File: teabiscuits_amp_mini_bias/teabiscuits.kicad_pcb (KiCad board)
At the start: 2 copper layers, 25 x 20 mm, 15 parts, among them J1 Conn_Coaxial, J2 Conn_Coaxial, J3 Conn_01x03_Male, J4 Conn_Coaxial, U2 LMP7721, U3 OP07

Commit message: Misc updates
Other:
- board text added: "TeaBisMB r2"
- board text removed: "TeaBisMB r1"
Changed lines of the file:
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@@
   (gr_line (start 152 140.75) (end 152 132.31) (layer Edge.Cuts) (width 0.05))
   (gr_line (start 177 128.75) (end 177 128.81) (layer Edge.Cuts) (width 0.05))
-  (gr_text "TeaBisMB r1" (at 156.5 143.25) (layer F.SilkS)
+  (gr_text "TeaBisMB r2" (at 156.5 143.25) (layer F.SilkS)
     (effects (font (size 0.5 0.5) (thickness 0.125)))
   )
@@
   (segment (start 165 142.6875) (end 165 142.475) (width 0.25) (layer B.Cu) (net 7))
   (segment (start 165 142.475) (end 165.5 141.975) (width 0.25) (layer B.Cu) (net 7))
-  (segment (start 170.55 130.56) (end 170.55 130.55) (width 0.25) (layer F.Cu) (net 12))
-  (segment (start 170.55 130.55) (end 170.5 130.5) (width 0.25) (layer F.Cu) (net 12))
   (segment (start 171 132.12) (end 171.481587 132.12) (width 0.25) (layer F.Cu) (net 11))
   (segment (start 171.481587 132.12) (end 171.886587 132.525) (width 0.25) (layer F.Cu) (net 11))
   (segment (start 158 132.12) (end 158 132.1) (width 0.25) (layer F.Cu) (net 11))
-  (via (at 175.75 144.5) (size 1.11) (drill 1.1) (layers F.Cu B.Cu) (net 11))
-  (via (at 175.75 127) (size 1.11) (drill 1.1) (layers F.Cu B.Cu) (net 11))
-  (via (at 153.25 127) (size 1.11) (drill 1.1) (layers F.Cu B.Cu) (net 11))
-  (via (at 153.25 144.5) (size 1.11) (drill 1.1) (layers F.Cu B.Cu) (net 11))
+  (via (at 175.75 144.5) (size 2.22) (drill 2.1) (layers F.Cu B.Cu) (net 11))
+  (via (at 175.75 127) (size 1.22) (drill 1.21) (layers F.Cu B.Cu) (net 11))
+  (via (at 153.25 127) (size 1.22) (drill 1.21) (layers F.Cu B.Cu) (net 11))
+  (via (at 153.25 144.5) (size 2.11) (drill 2.1) (layers F.Cu B.Cu) (net 11))
   (segment (start 171.025 134.74) (end 170.76 134.74) (width 0.25) (layer F.Cu) (net 11))
   (segment (start 170.76 134.74) (end 170.75 134.75) (width 0.25) (layer F.Cu) (net 11))
@@
   (segment (start 175.75 144.5) (end 153.25 144.5) (width 0.25) (layer F.Cu) (net 11))
   (segment (start 176.64999 145.39999) (end 175.75 144.5) (width 0.25) (layer F.Cu) (net 11))
+  (segment (start 170.55 130.56) (end 170.55 130.55) (width 0.25) (layer F.Cu) (net 12))
+  (segment (start 170.55 130.55) (end 170.5 130.5) (width 0.25) (layer F.Cu) (net 12))
   (segment (start 170.55 130.56) (end 169.31 130.56) (width 0.25) (layer F.Cu) (net 12))
   (via (at 169.25 130.5) (size 0.8) (drill 0.4) (layers F.Cu B.Cu) (net 12))

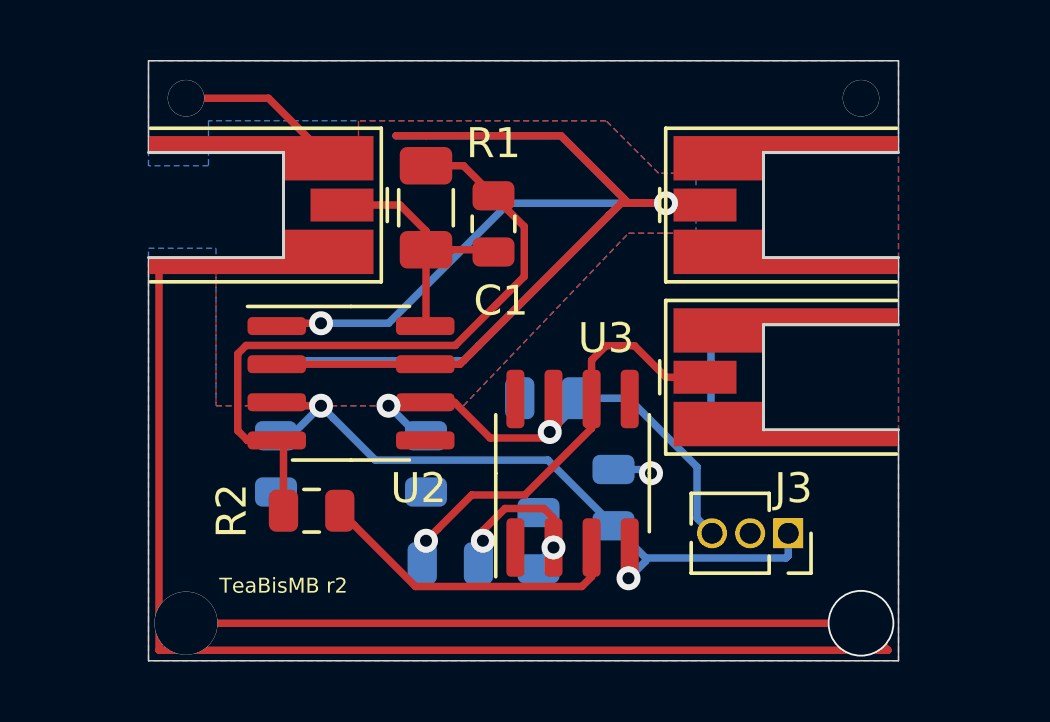
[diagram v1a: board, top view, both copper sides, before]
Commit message: Amplifier with bias updated to correct for offset
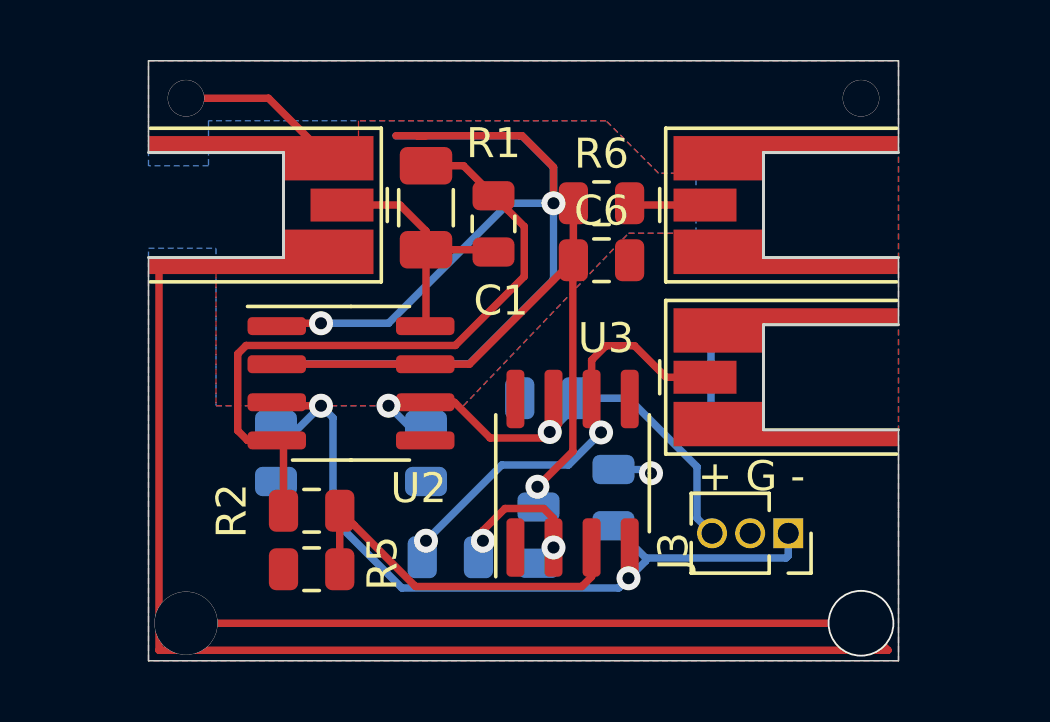
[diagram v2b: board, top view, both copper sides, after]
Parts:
- added C6: 100nF, Capacitor_SMD:C_0805_2012Metric, F.Cu at (167.1, 132.4)
- added R5: 1K, Resistor_SMD:R_0805_2012Metric, F.Cu at (157.4, 142.7)
- added R6: 1K, Resistor_SMD:R_0805_2012Metric, F.Cu at (167.1, 130.5)
- R3: value R -> 1K
- R4: value R -> 100
- moved C2 0.35 mm to (161.2, 138.8)
- moved C3 0.35 mm to (156.2, 138.8)
- moved R3 0.20 mm to (162.1, 142.3)
- moved R4 0.19 mm to (165.0, 141.6)
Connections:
- J4 pad 1: GUARD -> Net-(J4-Pad1)
- R4 pad 1: GND -> GUARD
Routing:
- net -5V: track 23.8 -> 27.3 mm
- net GUARD: track 64.3 -> 61.5 mm, vias 2 -> 3
- net Net-(J4-Pad1): track 0.00 -> 2.62 mm
- net Net-(R2-Pad1): track 10.6 -> 12.5 mm
- net Net-(J2-Pad1): track 15.2 -> 15.8 mm, vias 1 -> 2
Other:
- board text added: "+ G -"
- board text added: "TeaBisMB r3"
- board text removed: "TeaBisMB r2"

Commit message: r4 of integrated pcb
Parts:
- moved J2 3.05 mm to (176.3, 136.3)
- moved J4 3.05 mm to (176.3, 130.6)
- moved J1 2.95 mm to (152.8, 130.6)
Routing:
- net GND: track 79.0 -> 70.8 mm, vias 5 -> 6
- net Net-(J2-Pad1): track 15.8 -> 18.8 mm
- net Net-(J4-Pad1): track 2.62 -> 5.60 mm
- net Net-(C1-Pad2): track 9.31 -> 12.3 mm
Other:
- outline, holes or cut-outs redrawn
- board text added: "TeaBisMB r4"
- board text removed: "TeaBisMB r3"
